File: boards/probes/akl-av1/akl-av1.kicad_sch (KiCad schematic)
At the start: 20 parts, among them J2 TIPRES, J3 TIPRES, J4 SMPM, U4 BUF802

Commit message: Rev 0.2 of AKL-AV1
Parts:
- removed R12: 49.9, azonenberg_pcb:EIA_0402_RES_NOSILK, symbol device:R
- removed R9: 0, azonenberg_pcb:EIA_0402_RES_NOSILK, symbol device:R
- added C16: 800 fF, azonenberg_pcb:EIA_0402_CAP_NOSILK, symbol device:C
- R7: value DNP -> 1M; footprint azonenberg_pcb:EIA_0402_RES_NOSILK -> azonenberg_pcb:EIA_0402_CAP_NOSILK
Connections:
- net TIP: now also C16.1
- net VIN: now also R7.1, C16.2; no longer R7.2
- net at U4.3 (IN_BIAS): no longer R7.1
- net VAUX: no longer names the net of R11.2
- net VAUX: now also R7.2; no longer U4.4 (IN_AUX)
- no-connect marks 0 -> 3
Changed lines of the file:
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@@
 (kicad_sch (version 20211123) (generator eeschema)
   (paper "A4")
+  (title_block
+    (date "2022-06-21")
+    (rev "0.2")
+  )
   (junction (at 34.29 59.69) (diameter 0) (color 0 0 0 0)
   )
-  (junction (at 64.77 59.69) (diameter 0) (color 0 0 0 0)
-  )
   (junction (at 40.64 59.69) (diameter 0) (color 0 0 0 0)
   )
+  (junction (at 62.23 59.69) (diameter 0) (color 0 0 0 0)
+  )
   (junction (at 86.36 52.07) (diameter 0) (color 0 0 0 0)
   )
@@
   (junction (at 139.7 31.75) (diameter 0) (color 0 0 0 0)
   )
-  (junction (at 127 59.69) (diameter 0) (color 0 0 0 0)
-  )
   (junction (at 26.67 59.69) (diameter 0) (color 0 0 0 0)
   )
   (junction (at 154.94 46.99) (diameter 0) (color 0 0 0 0)
   )
+  (no_connect (at 86.36 64.77))
+  (no_connect (at 86.36 62.23))
+  (no_connect (at 86.36 41.91))
   (wire (pts (xy 86.36 49.53) (xy 86.36 52.07))
     (stroke (width 0) (type default) (color 0 0 0 0))
   )
-  (wire (pts (xy 52.07 83.82) (xy 52.07 62.23))
-    (stroke (width 0) (type default) (color 0 0 0 0))
-  )
   (wire (pts (xy 34.29 59.69) (xy 40.64 59.69))
     (stroke (width 0) (type default) (color 0 0 0 0))
   )
-  (wire (pts (xy 127 59.69) (xy 139.7 59.69))
+  (wire (pts (xy 124.46 59.69) (xy 139.7 59.69))
     (stroke (width 0) (type default) (color 0 0 0 0))
   )
@@
     (stroke (width 0) (type default) (color 0 0 0 0))
   )
+  (wire (pts (xy 62.23 83.82) (xy 52.07 83.82))
+    (stroke (width 0) (type default) (color 0 0 0 0))
+  )
   (wire (pts (xy 125.73 46.99) (xy 139.7 46.99))
     (stroke (width 0) (type default) (color 0 0 0 0))
@@
     (stroke (width 0) (type default) (color 0 0 0 0))
   )
-  (wire (pts (xy 78.74 41.91) (xy 86.36 41.91))
+  (wire (pts (xy 62.23 67.31) (xy 62.23 83.82))
+    (stroke (width 0) (type default) (color 0 0 0 0))
+  )
+  (wire (pts (xy 26.67 49.53) (xy 26.67 59.69))
+    (stroke (width 0) (type default) (color 0 0 0 0))
+  )
+  (wire (pts (xy 62.23 59.69) (xy 86.36 59.69))
     (stroke (width 0) (type default) (color 0 0 0 0))
   )
@@
     (stroke (width 0) (type default) (color 0 0 0 0))
   )
-  (wire (pts (xy 124.46 67.31) (xy 127 67.31))
-    (stroke (width 0) (type default) (color 0 0 0 0))
-  )
   (wire (pts (xy 139.7 31.75) (xy 154.94 31.75))
     (stroke (width 0) (type default) (color 0 0 0 0))
@@
     (stroke (width 0) (type default) (color 0 0 0 0))
   )
-  (wire (pts (xy 72.39 64.77) (xy 86.36 64.77))
+  (wire (pts (xy 34.29 49.53) (xy 34.29 59.69))
     (stroke (width 0) (type default) (color 0 0 0 0))
   )
@@
     (stroke (width 0) (type default) (color 0 0 0 0))
   )
-  (wire (pts (xy 64.77 59.69) (xy 64.77 64.77))
-    (stroke (width 0) (type default) (color 0 0 0 0))
-  )
-  (wire (pts (xy 124.46 59.69) (xy 127 59.69))
-    (stroke (width 0) (type default) (color 0 0 0 0))
-  )
   (wire (pts (xy 26.67 59.69) (xy 26.67 68.58))
     (stroke (width 0) (type default) (color 0 0 0 0))
   )
-  (wire (pts (xy 52.07 62.23) (xy 86.36 62.23))
-    (stroke (width 0) (type default) (color 0 0 0 0))
-  )
-  (wire (pts (xy 64.77 59.69) (xy 86.36 59.69))
-    (stroke (width 0) (type default) (color 0 0 0 0))
-  )
-  (wire (pts (xy 40.64 59.69) (xy 64.77 59.69))
+  (wire (pts (xy 40.64 59.69) (xy 62.23 59.69))
     (stroke (width 0) (type default) (color 0 0 0 0))
   )
@@
     (effects (font (size 1.27 1.27)) (justify left bottom))
   )
-  (label "VAUX" (at 52.07 62.23 0)
-    (effects (font (size 1.27 1.27)) (justify left bottom))
-  )
   (label "4V5_N" (at 125.73 46.99 180)
     (effects (font (size 1.27 1.27)) (justify right bottom))
@@
     (effects (font (size 1.27 1.27)) (justify left bottom))
   )
-  (label "GND" (at 124.46 67.31 180)
-    (effects (font (size 1.27 1.27)) (justify right bottom))
-  )
   (label "4V5_P" (at 86.36 72.39 180)
     (effects (font (size 1.27 1.27)) (justify right bottom))
@@
     (effects (font (size 1.27 1.27)) (justify right bottom))
   )
-  (label "4V5_N" (at 71.12 41.91 180)
-    (effects (font (size 1.27 1.27)) (justify right bottom))
-  )
   (label "4V5_P" (at 30.48 20.32 0)
     (effects (font (size 1.27 1.27)) (justify left bottom))
@@
     (pin "2")
   )
-  (symbol (lib_id "device:R") (at 127 63.5 180) (unit 1)
-    (in_bom yes) (on_board yes) (fields_autoplaced)
-    (property "Reference" "R12" (id 0) (at 128.778 62.5915 0)
-      (effects (font (size 1.27 1.27)) (justify right))
-    )
-    (property "Value" "49.9" (id 1) (at 128.778 65.3666 0)
-      (effects (font (size 1.27 1.27)) (justify right))
-    )
-    (property "Footprint" "azonenberg_pcb:EIA_0402_RES_NOSILK" (id 2) (at 128.778 63.5 90)
-      (effects (font (size 1.27 1.27)) hide)
-    )
-    (property "Datasheet" "" (id 3) (at 127 63.5 0)
-      (effects (font (size 1.27 1.27)) hide)
-    )
-    (pin "1")
-    (pin "2")
-  )
   (symbol (lib_id "device:C") (at 139.7 43.18 0) (unit 1)
     (in_bom yes) (on_board yes) (fields_autoplaced)
@@
     )
     (property "Datasheet" "" (id 3) (at 139.7 43.18 0)
-      (effects (font (size 1.27 1.27)) hide)
-    )
-    (pin "1")
-    (pin "2")
-  )
-  (symbol (lib_id "device:R") (at 74.93 41.91 90) (unit 1)
-    (in_bom yes) (on_board yes)
-    (property "Reference" "R9" (id 0) (at 74.93 36.9275 90))
-    (property "Value" "0" (id 1) (at 74.93 41.91 90))
-    (property "Footprint" "azonenberg_pcb:EIA_0402_RES_NOSILK" (id 2) (at 74.93 43.688 90)
-      (effects (font (size 1.27 1.27)) hide)
-    )
-    (property "Datasheet" "" (id 3) (at 74.93 41.91 0)
       (effects (font (size 1.27 1.27)) hide)
     )
@@
     )
     (property "Datasheet" "" (id 3) (at 125.73 35.56 0)
+      (effects (font (size 1.27 1.27)) hide)
+    )
+    (pin "1")
+    (pin "2")
+  )
+  (symbol (lib_id "device:R") (at 62.23 63.5 0) (unit 1)
+    (in_bom yes) (on_board yes) (fields_autoplaced)
+    (property "Reference" "R7" (id 0) (at 64.008 62.5915 0)
+      (effects (font (size 1.27 1.27)) (justify left))
+    )
+    (property "Value" "1M" (id 1) (at 64.008 65.3666 0)
+      (effects (font (size 1.27 1.27)) (justify left))
+    )
+    (property "Footprint" "azonenberg_pcb:EIA_0402_CAP_NOSILK" (id 2) (at 60.452 63.5 90)
+      (effects (font (size 1.27 1.27)) hide)
+    )
+    (property "Datasheet" "" (id 3) (at 62.23 63.5 0)
       (effects (font (size 1.27 1.27)) hide)
     )
@@
     (pin "2")
   )
-  (symbol (lib_id "device:R") (at 68.58 64.77 270) (unit 1)
-    (in_bom yes) (on_board yes)
-    (property "Reference" "R7" (id 0) (at 68.58 67.31 90))
-    (property "Value" "DNP" (id 1) (at 68.58 64.77 90))
-    (property "Footprint" "azonenberg_pcb:EIA_0402_RES_NOSILK" (id 2) (at 68.58 62.992 90)
-      (effects (font (size 1.27 1.27)) hide)
-    )
-    (property "Datasheet" "" (id 3) (at 68.58 64.77 0)
-      (effects (font (size 1.27 1.27)) hide)
-    )
-    (pin "1")
-    (pin "2")
-  )
   (symbol (lib_id "device:C") (at 154.94 35.56 0) (unit 1)
     (in_bom yes) (on_board yes) (fields_autoplaced)
@@
     )
     (pin "1")
+  )
+  (symbol (lib_id "device:C") (at 30.48 49.53 90) (unit 1)
+    (in_bom yes) (on_board yes) (fields_autoplaced)
+    (property "Reference" "C16" (id 0) (at 30.48 43.4045 90))
+    (property "Value" "800 fF" (id 1) (at 30.48 46.1796 90))
+    (property "Footprint" "azonenberg_pcb:EIA_0402_CAP_NOSILK" (id 2) (at 34.29 48.5648 0)
+      (effects (font (size 1.27 1.27)) hide)
+    )
+    (property "Datasheet" "" (id 3) (at 30.48 49.53 0)
+      (effects (font (size 1.27 1.27)) hide)
+    )
+    (pin "1")
+    (pin "2")
   )
   (symbol (lib_id "device:R") (at 30.48 59.69 90) (unit 1)
@@
       (reference "C15") (unit 1) (value "0.47 uF") (footprint "azonenberg_pcb:EIA_0402_CAP_NOSILK")
     )
+    (path "/f0f3907b-44e3-4106-9f24-d8ce836b6bb0"
+      (reference "C16") (unit 1) (value "800 fF") (footprint "azonenberg_pcb:EIA_0402_CAP_NOSILK")
+    )
     (path "/a12b751e-ae7a-468c-af3d-31ed4d501b01/01b78dbf-3409-41aa-9496-f65444fa6c41"
       (reference "J1") (unit 1) (value "U.FL") (footprint "azonenberg_pcb:CONN_U.FL_TE_1909763-1")
@@
       (reference "J4") (unit 1) (value "SMPM") (footprint "azonenberg_pcb:CONN_SMPM_AMPHENOL_925-169J-51PT")
     )
+    (path "/a12b751e-ae7a-468c-af3d-31ed4d501b01/cc42285d-e5b0-450b-ad46-b9ca27c6c5ee"
+      (reference "L1") (unit 1) (value "FERRITE") (footprint "azonenberg_pcb:EIA_0402_CAP_NOSILK")
+    )
     (path "/a12b751e-ae7a-468c-af3d-31ed4d501b01/a59a409d-ee44-4464-b670-4d6186d855cf"
       (reference "R1") (unit 1) (value "88.7K") (footprint "azonenberg_pcb:EIA_0402_RES_NOSILK")
@@
       (reference "R6") (unit 1) (value "1M") (footprint "azonenberg_pcb:EIA_0402_RES_NOSILK")
     )
-    (path "/be1ae09e-9a6a-439e-8c73-0e39b5b85f13"
-      (reference "R7") (unit 1) (value "DNP") (footprint "azonenberg_pcb:EIA_0402_RES_NOSILK")
+    (path "/9e295006-012e-4c5f-853e-07dac10c3673"
+      (reference "R7") (unit 1) (value "1M") (footprint "azonenberg_pcb:EIA_0402_CAP_NOSILK")
     )
     (path "/d63c2882-db11-411e-85a9-c04372d71b25"
       (reference "R8") (unit 1) (value "17.8K") (footprint "azonenberg_pcb:EIA_0402_RES_NOSILK")
     )
-    (path "/5839aa7d-a087-48e3-8477-f6ab730e86e6"
-      (reference "R9") (unit 1) (value "0") (footprint "azonenberg_pcb:EIA_0402_RES_NOSILK")
-    )
     (path "/607dcca5-fd89-4480-b765-a49277ef4ef3"
       (reference "R10") (unit 1) (value "49.9") (footprint "azonenberg_pcb:EIA_0402_RES_NOSILK")
@@
       (reference "R11") (unit 1) (value "3312J-1-103E1") (footprint "azonenberg_pcb:RES_TRIM_BOURNS_3312")
     )
-    (path "/309388ab-a6f2-4c4d-bb54-82c7b9e67025"
-      (reference "R12") (unit 1) (value "49.9") (footprint "azonenberg_pcb:EIA_0402_RES_NOSILK")
-    )
     (path "/a12b751e-ae7a-468c-af3d-31ed4d501b01/16ec4fd1-5016-48c9-8166-01e39101d830"

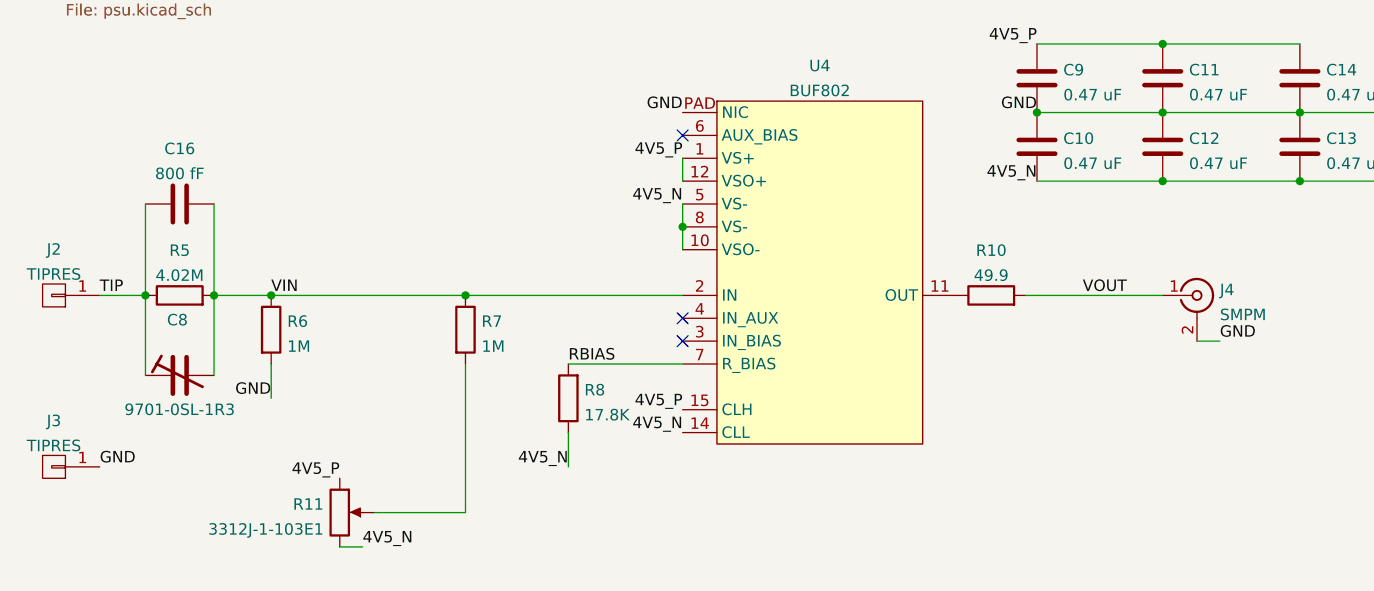
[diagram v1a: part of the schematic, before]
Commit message: Began work on AKL-AV1 v0.3 ECOs
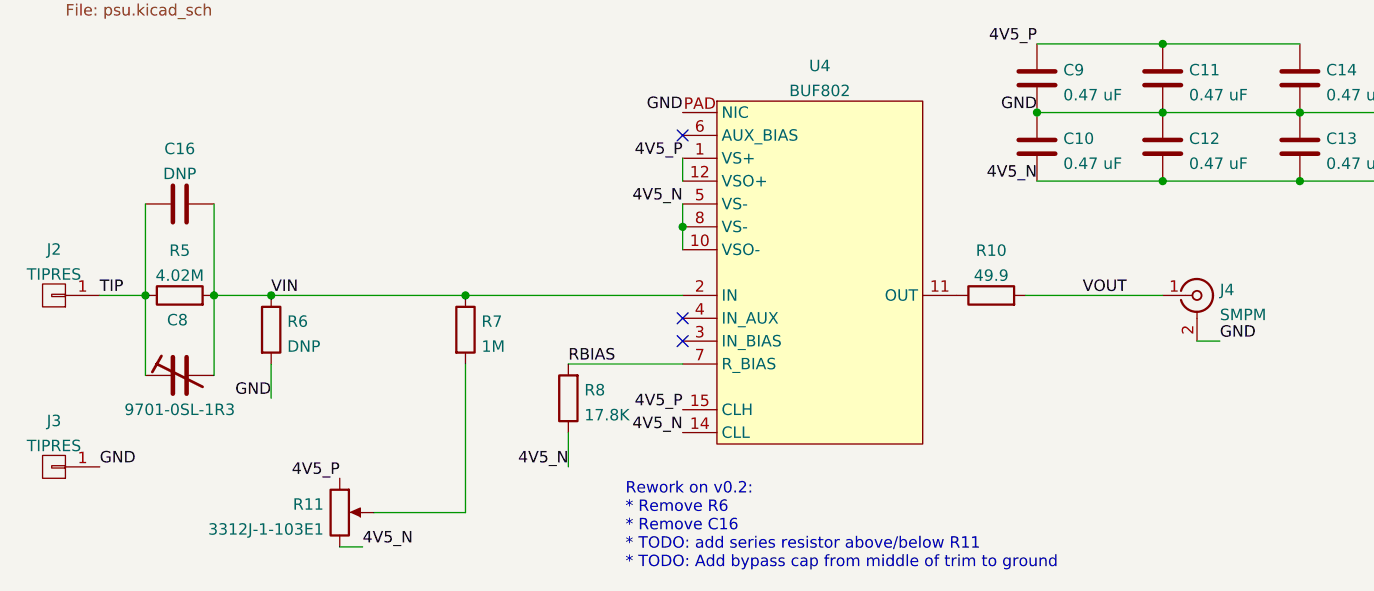
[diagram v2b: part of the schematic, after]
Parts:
- C16: value 800 fF -> DNP
- R6: value 1M -> DNP
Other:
- note added: "Rework on v0.2: * Remove R6 * Remove C16 * TODO: add series resistor above/below R11 * TODO: Add bypass cap from middle of trim to ground"
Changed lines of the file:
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@@
     (stroke (width 0) (type default) (color 0 0 0 0))
+  )
+  (text "Rework on v0.2:\n* Remove R6\n* Remove C16\n* TODO: add series resistor above/below R11\n* TODO: Add bypass cap from middle of trim to ground"
+    (at 80.01 90.17 0)
+    (effects (font (size 1.27 1.27)) (justify left bottom))
   )
   (label "4V5_N" (at 30.48 25.4 0)
@@
       (effects (font (size 1.27 1.27)) (justify left))
     )
-    (property "Value" "1M" (id 1) (at 42.418 65.3666 0)
+    (property "Value" "DNP" (id 1) (at 42.418 65.3666 0)
       (effects (font (size 1.27 1.27)) (justify left))
     )
@@
     (in_bom yes) (on_board yes) (fields_autoplaced)
     (property "Reference" "C16" (id 0) (at 30.48 43.4045 90))
-    (property "Value" "800 fF" (id 1) (at 30.48 46.1796 90))
+    (property "Value" "DNP" (id 1) (at 30.48 46.1796 90))
     (property "Footprint" "azonenberg_pcb:EIA_0402_CAP_NOSILK" (id 2) (at 34.29 48.5648 0)
       (effects (font (size 1.27 1.27)) hide)
@@
     )
     (path "/f0f3907b-44e3-4106-9f24-d8ce836b6bb0"
-      (reference "C16") (unit 1) (value "800 fF") (footprint "azonenberg_pcb:EIA_0402_CAP_NOSILK")
+      (reference "C16") (unit 1) (value "DNP") (footprint "azonenberg_pcb:EIA_0402_CAP_NOSILK")
     )
     (path "/a12b751e-ae7a-468c-af3d-31ed4d501b01/01b78dbf-3409-41aa-9496-f65444fa6c41"
@@
     )
     (path "/d763b496-b309-4766-860e-8c52275e77b8"
-      (reference "R6") (unit 1) (value "1M") (footprint "azonenberg_pcb:EIA_0402_RES_NOSILK")
+      (reference "R6") (unit 1) (value "DNP") (footprint "azonenberg_pcb:EIA_0402_RES_NOSILK")
     )
     (path "/9e295006-012e-4c5f-853e-07dac10c3673"

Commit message: Updated AKL-AV1 design files for v0.3 prototype
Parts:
- removed R11: 3312J-1-103E1, azonenberg_pcb:RES_TRIM_BOURNS_3312, symbol device:POT
- added C17: 0.47 uF, azonenberg_pcb:EIA_0402_CAP_NOSILK, symbol device:C
- added C18: 56 pF, azonenberg_pcb:EIA_0402_CAP_NOSILK, symbol device:C
- added C19: 330 pF, azonenberg_pcb:EIA_0402_CAP_NOSILK, symbol device:C
- added C20: 100 pF, azonenberg_pcb:EIA_0402_CAP_NOSILK, symbol device:C
- added R11: 30, azonenberg_pcb:EIA_0402_RES_NOSILK, symbol device:R
- added R12: 80.6K, azonenberg_pcb:EIA_0402_RES_NOSILK, symbol device:R
- added R13: 2K, azonenberg_pcb:EIA_0402_RES_NOSILK, symbol device:R
- added R14: 10M, azonenberg_pcb:EIA_0402_RES_NOSILK, symbol device:R
- added R9: 3312J-1-203E, azonenberg_pcb:RES_TRIM_BOURNS_3312, symbol device:POT
- added U5: ADA4075-2, azonenberg_pcb:DFN_8_0.5MM_2x2MM_NOPAD, symbol analog-azonenberg:ADA4075-2
- C16: value DNP -> 0.47 uF
- R6: value DNP -> 806K
- R7: value 1M -> 200K; footprint azonenberg_pcb:EIA_0402_CAP_NOSILK -> azonenberg_pcb:EIA_0402_RES_NOSILK
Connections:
- net 4V5_N: now also U4.6 (AUX_BIAS), C17.2, U5.4 (V-)
- net 4V5_P: now also C16.1, U5.8 (V+)
- net GND: now also C16.2, R7.2, C17.1, C20.2, R9.2, U5.5 (+INB), U5.6 (-INB); no longer R6.2
- net TIP: no longer C16.1
- net VIN: now also R11.1; no longer C16.2, R7.1, U4.2 (IN)
- net at R10.1, U4.11 (OUT): now also R12.2
- net at U4.3 (IN_BIAS): now also R14.2
- net VAUX: now reaches U4.4 (IN_AUX)
- net VAUX: now also C20.1, R13.2
- new net: C18.1, R12.1, R9.1, U5.2 (-INA)
- new net: C18.2, R13.1, U5.1 (OUTA)
- new net: C19.1, R11.2
- new net: R6.2, R7.1, U5.3 (+INA)
- new net: C19.2, R14.1, U4.2 (IN)
- no-connect marks 3 -> 2
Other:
- note added: "gain is alpha / beta alpha = 800k/200k beta = 80k/(variable 20k) alpha / beta = G = 0.97"
- note removed: "Rework on v0.2: * Remove R6 * Remove C16 * TODO: add series resistor above/below R11 * TODO: Add bypass cap from middle of trim to ground"
- moved on the sheet: C10, C11, C12, C13, C14, C15, C9, J4, R10, R8, U4
